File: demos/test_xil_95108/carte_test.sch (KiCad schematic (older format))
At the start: 42 parts, among them J1 DB25, J2 DB9FEM, K1 CONN_3, P2 CONN_3, P3 CONN_2, P4 CONN_2X2, SW1 SW_PUSH, SW2 SW_PUSH, U1 TDA8702, U2 XC95108PC84, U3 LM7805, U4 74HC04, U5 RAM_32KO, U6 LM318N, X1 10MHz

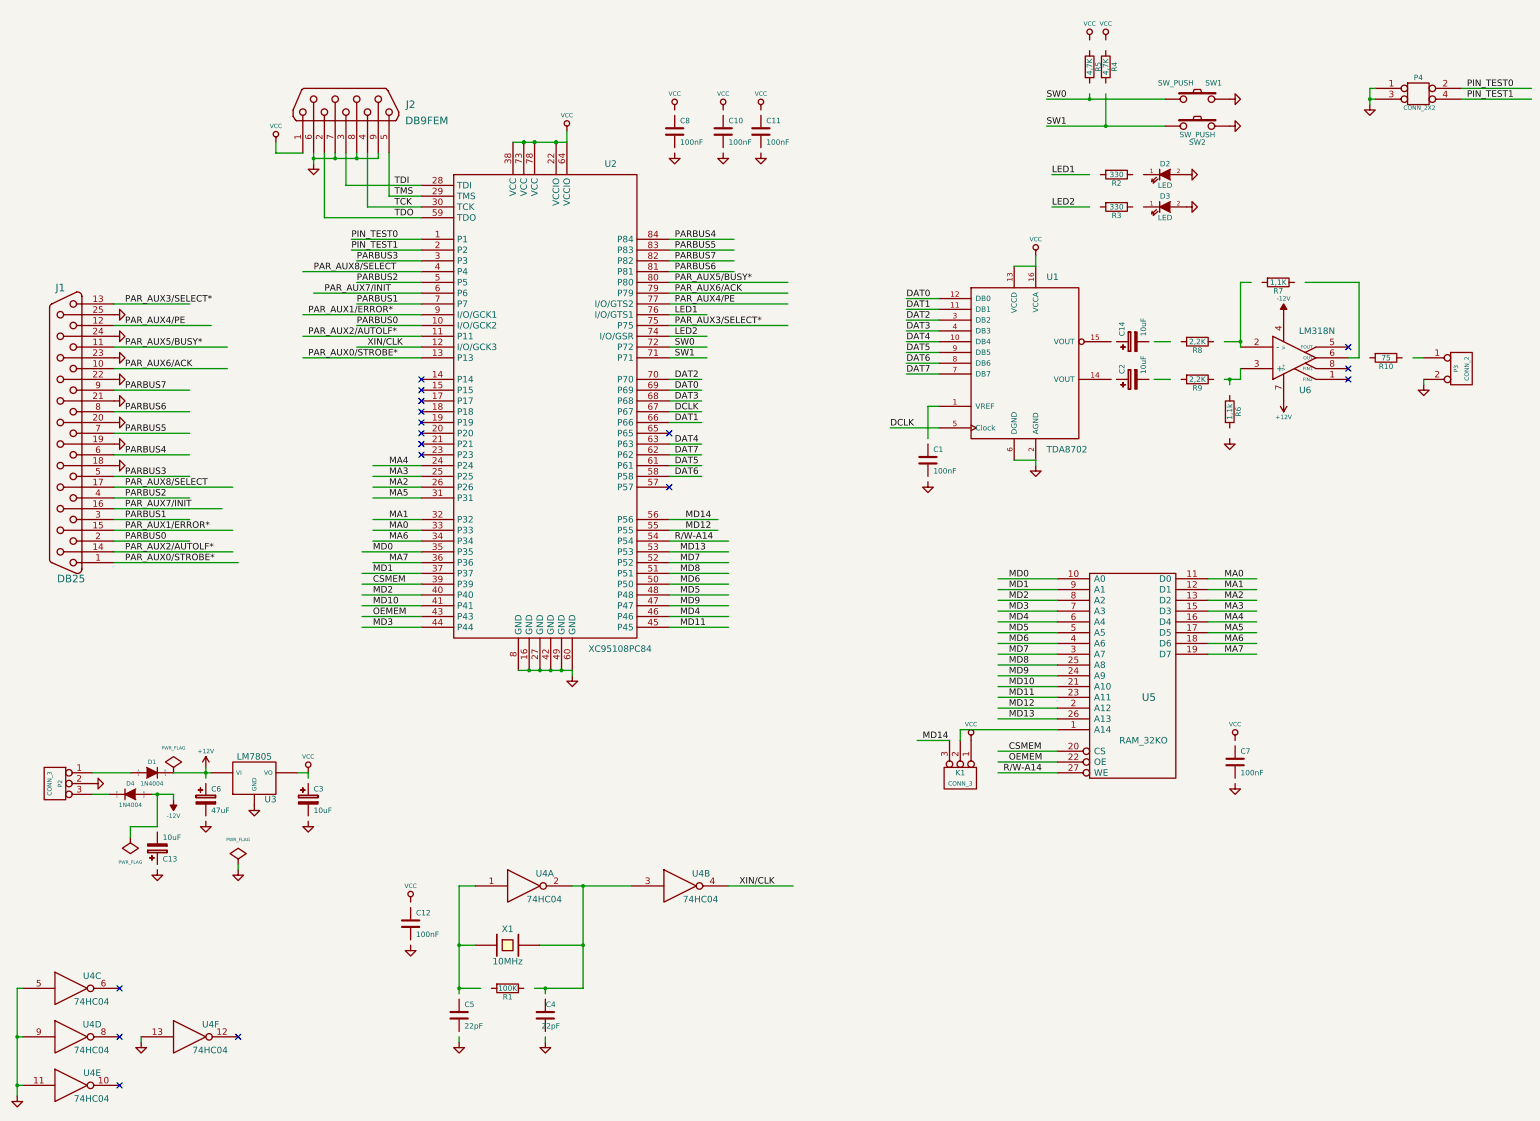
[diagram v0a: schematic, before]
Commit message: Update demo files. A minor code cleaning.
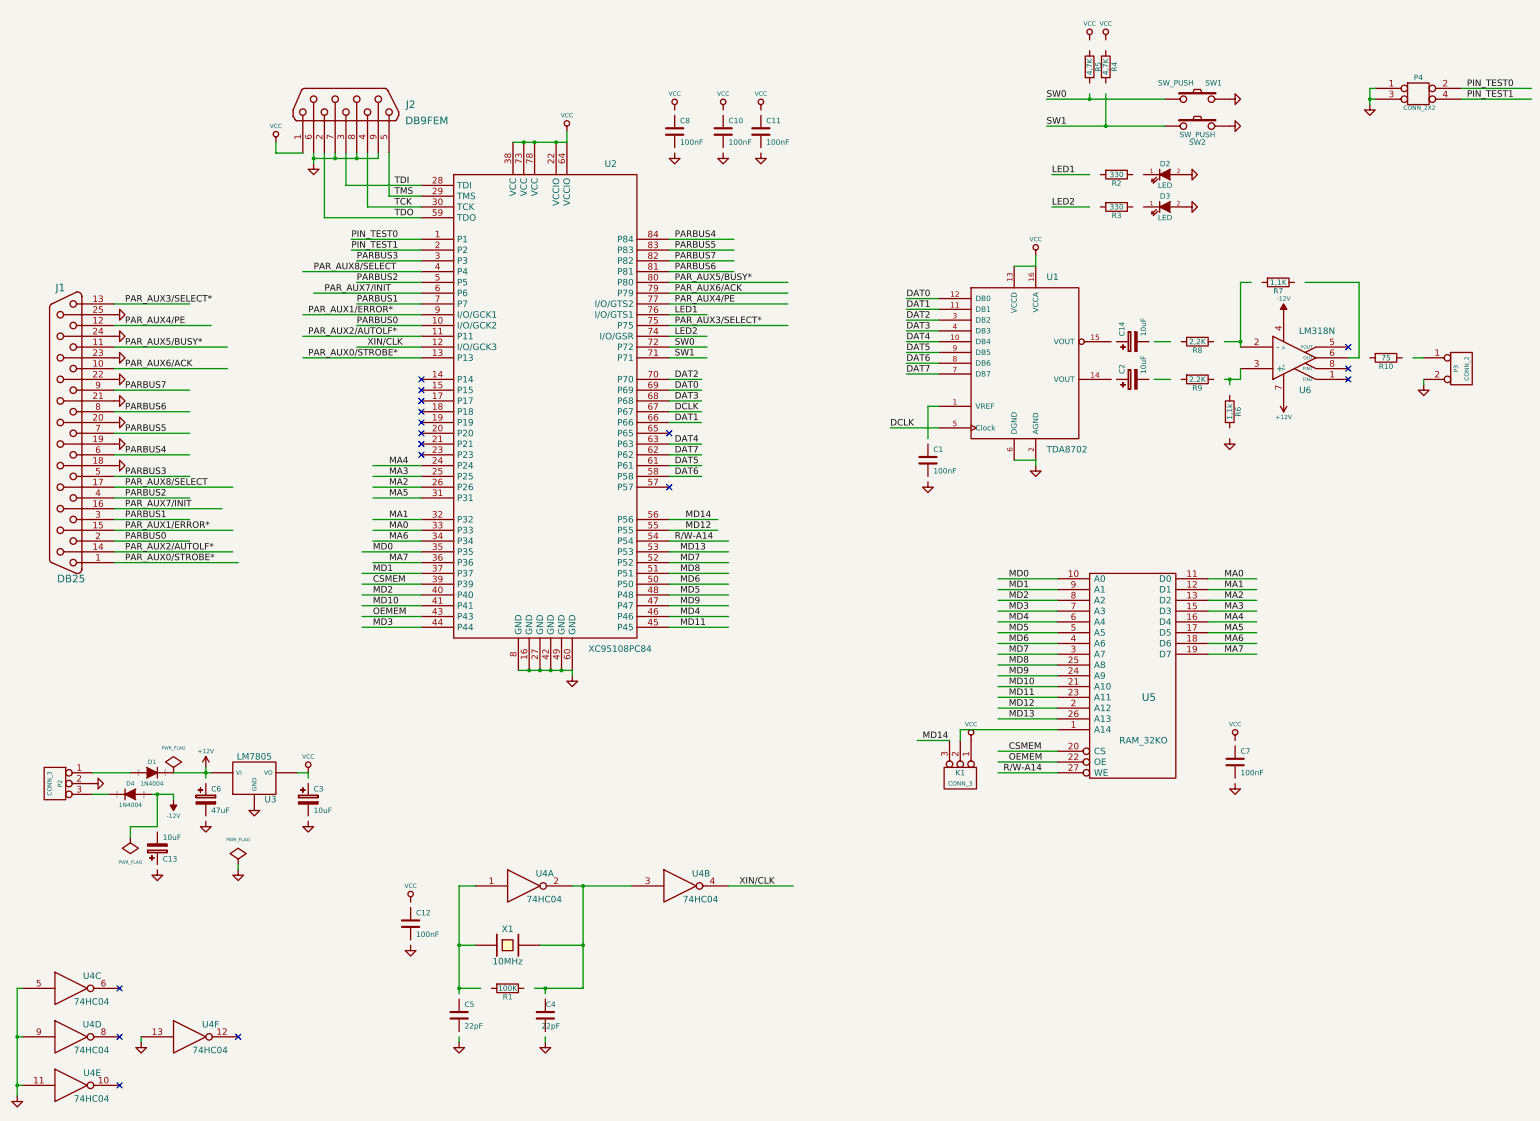
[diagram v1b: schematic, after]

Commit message: demos/ schematic tidying
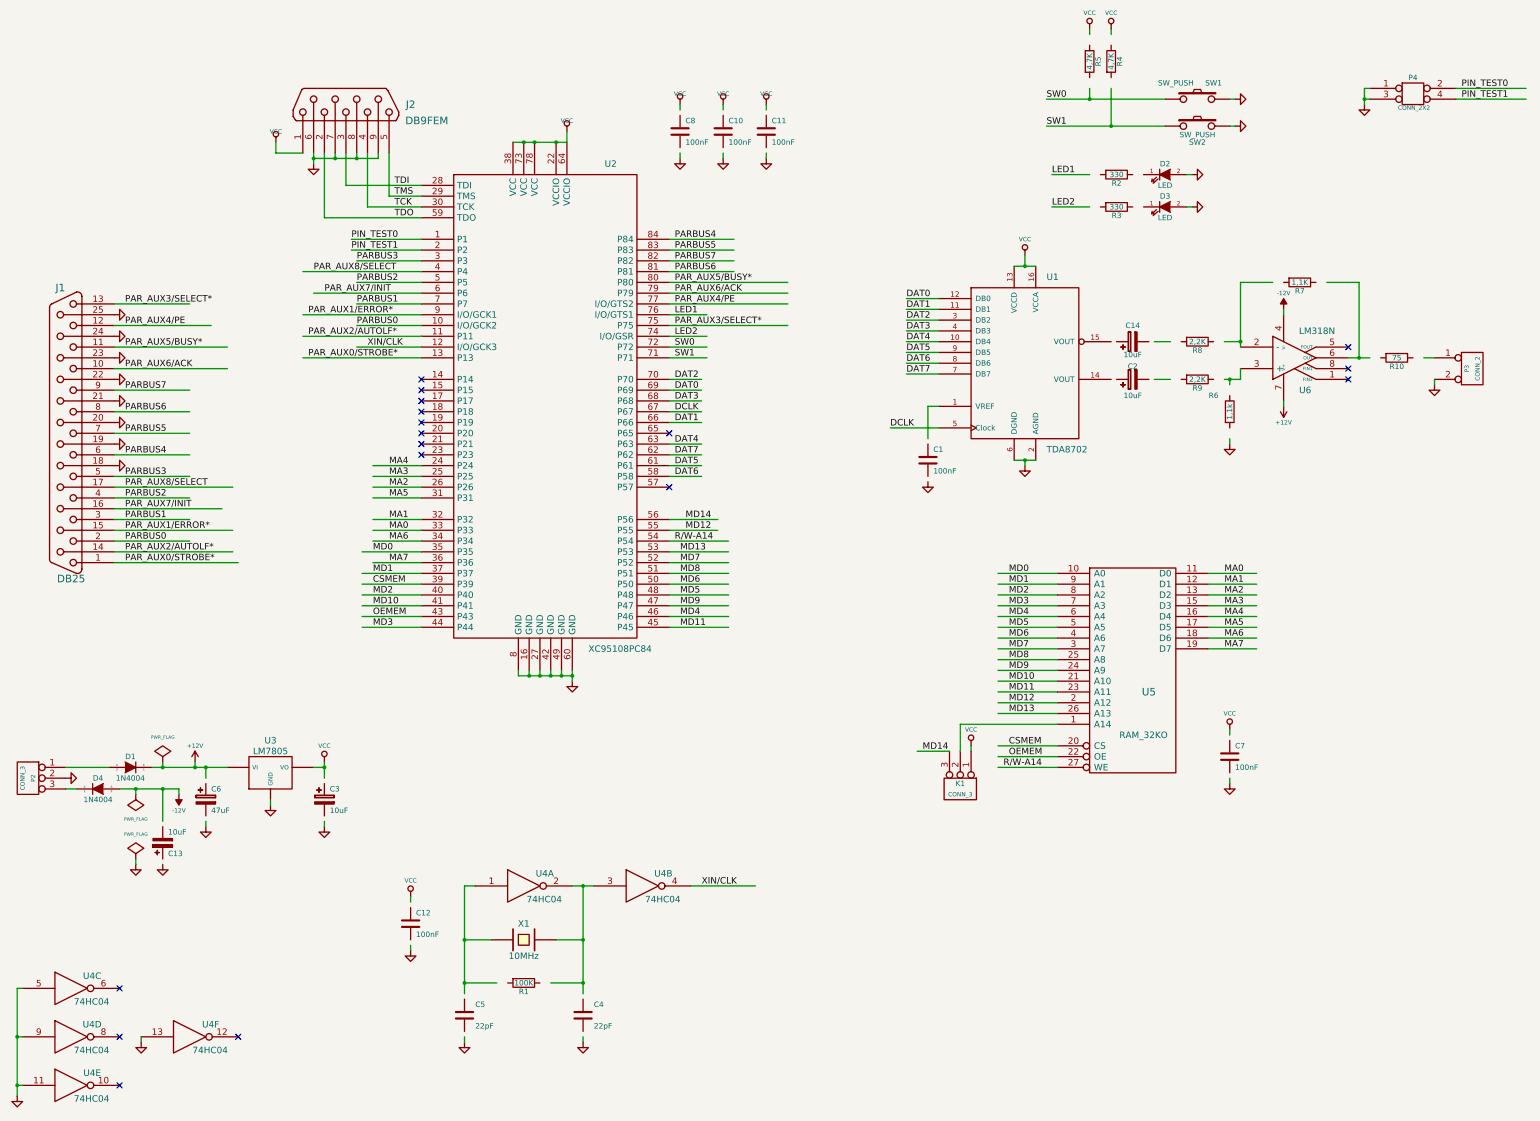
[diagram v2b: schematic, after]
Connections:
- wire segments 191 -> 251
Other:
- moved on the sheet: C11, C13, C3, C4, C5, C7, C8, D1, D4, K1, P2, P3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

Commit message: Footprint wizard: fixes and enhancements in python scripts.
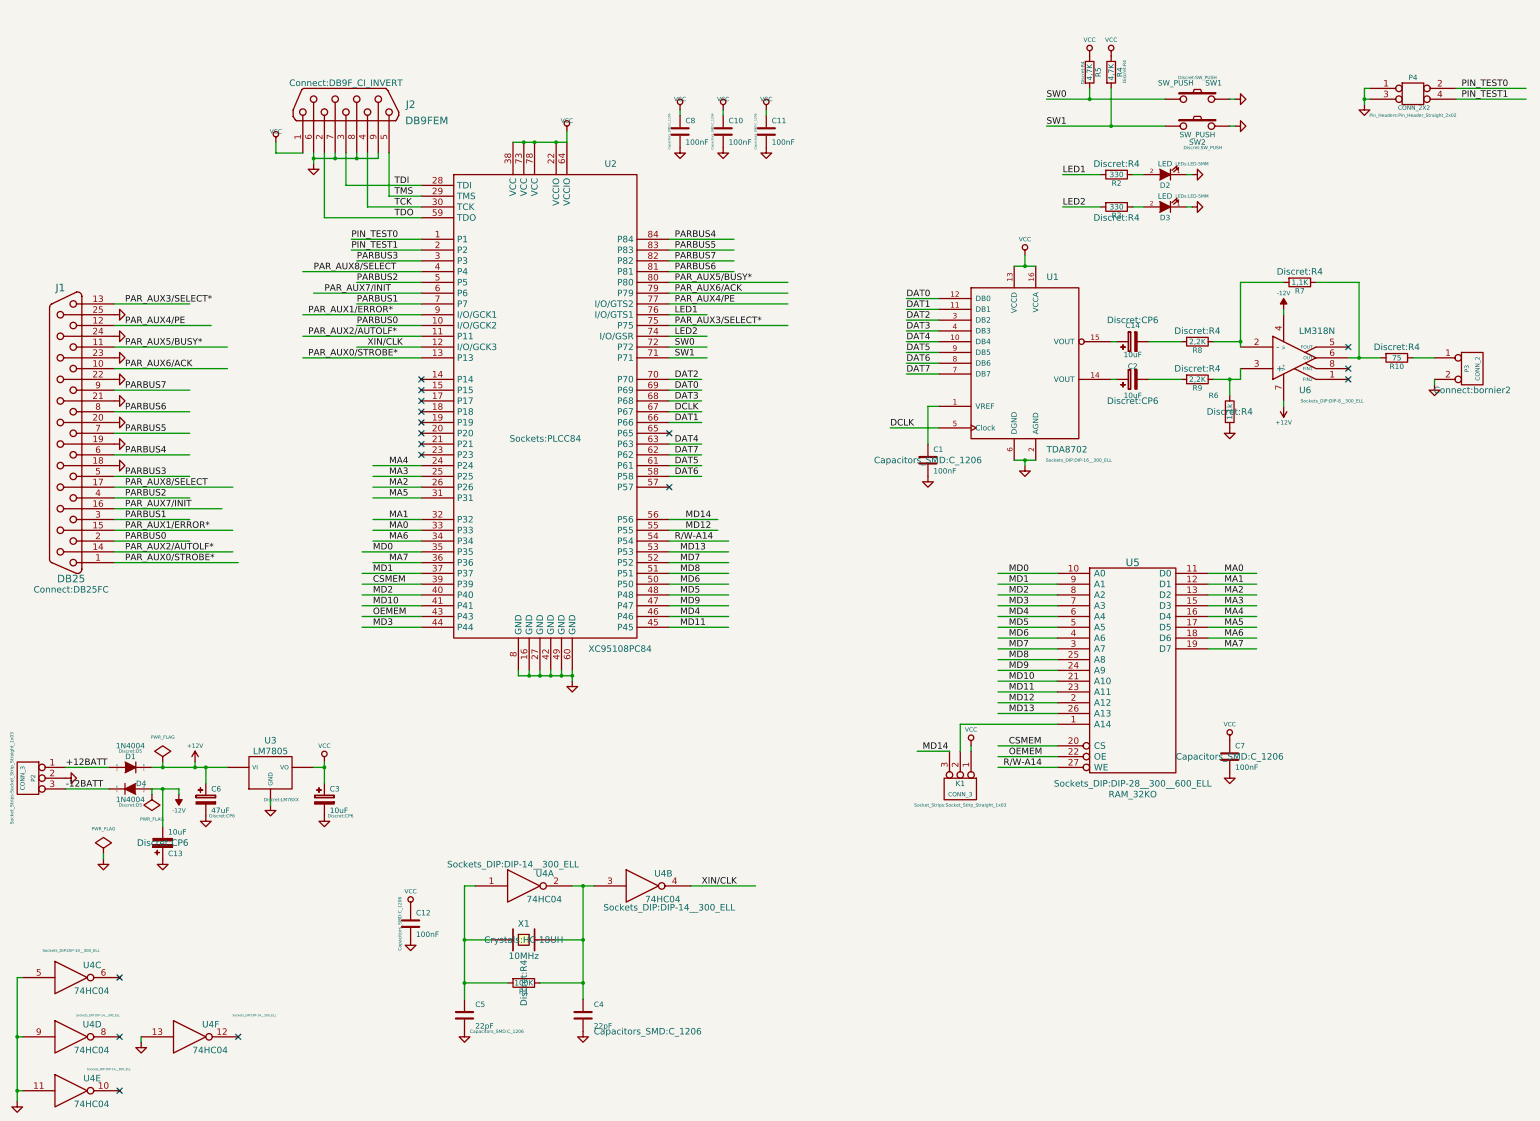
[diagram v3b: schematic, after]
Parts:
- C1, C10, C11, C12, C4, C5, C7, C8: footprint (none) -> Capacitors_SMD:C_1206
- C13, C14, C2, C3, C6: footprint (none) -> Discret:CP6
- D1, D4: footprint (none) -> Discret:D5
- D2, D3: footprint (none) -> LEDs:LED-5MM
- J1: footprint (none) -> Connect:DB25FC
- J2: footprint (none) -> Connect:DB9F_CI_INVERT
- K1, P2: footprint (none) -> Socket_Strips:Socket_Strip_Straight_1x03
- P3: footprint (none) -> Connect:bornier2
- P4: footprint (none) -> Pin_Headers:Pin_Header_Straight_2x02
- R1, R10, R2, R3, R4, R5, R6, R7, R8, R9: footprint (none) -> Discret:R4
- SW1, SW2: footprint (none) -> Discret:SW_PUSH
- U1: footprint (none) -> Sockets_DIP:DIP-16__300_ELL
- U2: footprint (none) -> Sockets:PLCC84
- U3: footprint (none) -> Discret:LM78XX
- U4: footprint (none) -> Sockets_DIP:DIP-14__300_ELL
- U5: footprint (none) -> Sockets_DIP:DIP-28__300__600_ELL
- U6: footprint (none) -> Sockets_DIP:DIP-8__300_ELL
- X1: footprint (none) -> Crystals:HC-18UH
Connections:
- net labels added: +12BATT, -12BATT
- wire segments 251 -> 209
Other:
- moved on the sheet: D4, R4, R5, U4C, U4E

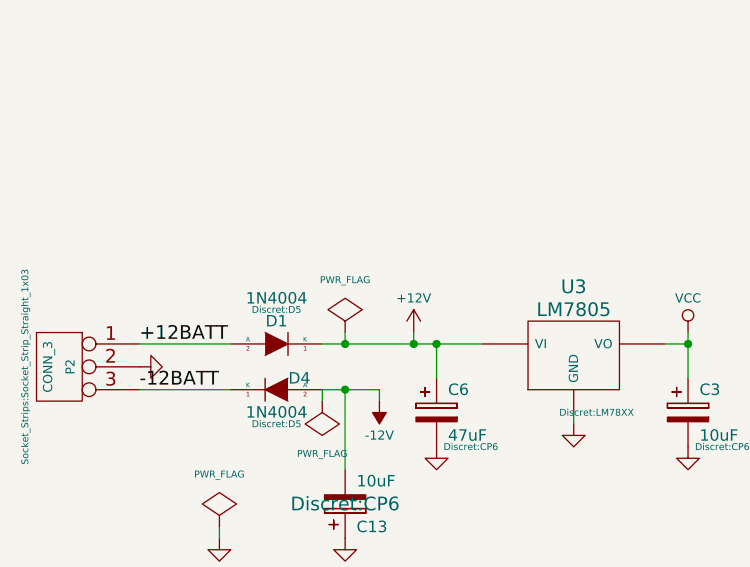
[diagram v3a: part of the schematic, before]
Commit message: polygons in footprint body: fix incorrect calculation of polygons with clearance or outline thickness (fix bug #1511366) Clean demos
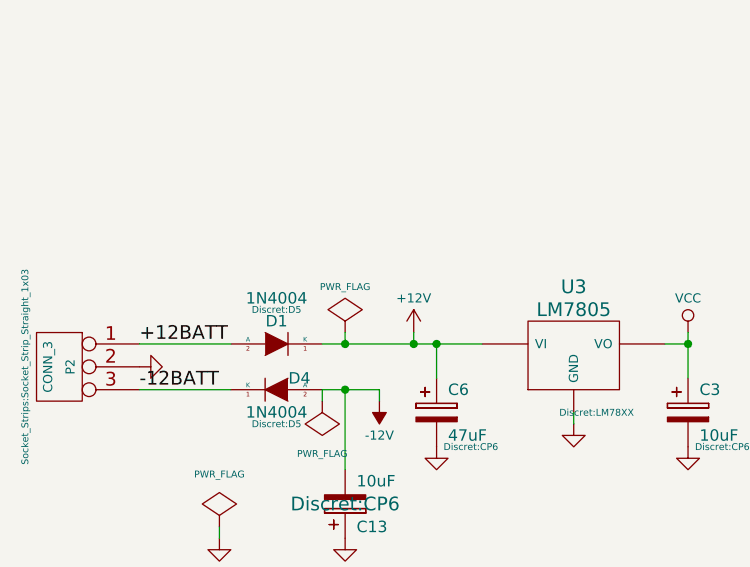
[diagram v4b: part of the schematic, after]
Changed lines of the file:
@@
 P 2400 7750
 F 0 "#FLG01" H 2400 8020 30  0001 C CNN
-F 1 "PWR_FLAG" H 2400 7980 30  0000 C CNN
+F 1 "PWR_FLAG" H 2400 7950 30  0000 C CNN
 F 2 "" H 2400 7750 60  0001 C CNN
 F 3 "" H 2400 7750 60  0001 C CNN
